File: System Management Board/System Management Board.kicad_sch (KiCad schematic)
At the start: 138 parts, among them IC1 SI2318CDS-T1-GE3, IC2 SI2318CDS-T1-GE3, IC3 SI2318CDS-T1-GE3, IC4 SI2318CDS-T1-GE3, IC5 SI2318CDS-T1-GE3, IC6 SI2318CDS-T1-GE3, J1 Conn_01x04_Male, J10 Conn_01x02_Male, J11 Conn_02x20_Odd_Even, J12 Conn_02x05_Top_Bottom, J13 Conn_01x04_Female, J2 Conn_01x04_Male, J3 Conn_01x02_Male, J4 PJ-063BH, J5 Conn_01x02_Male, J6 Conn_02x06_Counter_Clockwise, J7 Conn_02x20_Odd_Even, J8 Conn_01x02_Male, J9 Conn_01x02_Male, K1 J115F11CH5VDCS61.5U, K2 J114FL1CS165VDC.41, K3 J114FL1CS165VDC.41, SW1 SW_Push, SW2 SW_Push, U1 SC0915, U4 R1560J501B-T1-YE, U5 74HC4051, U6 MCP9700T-ETT, U7 MCP9700T-ETT

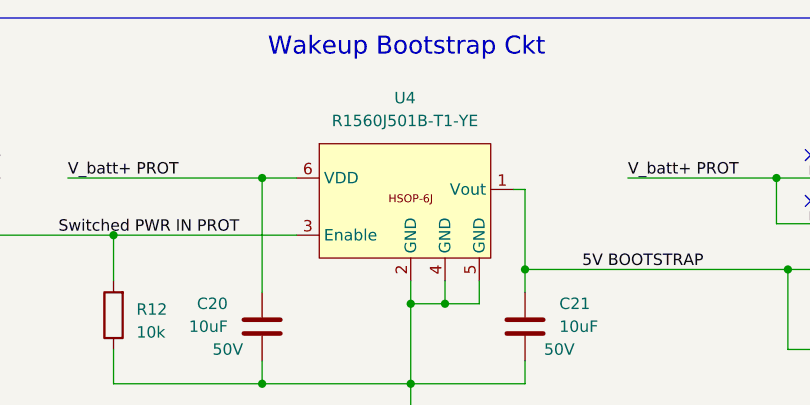
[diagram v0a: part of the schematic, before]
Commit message: minor changes naming or routing
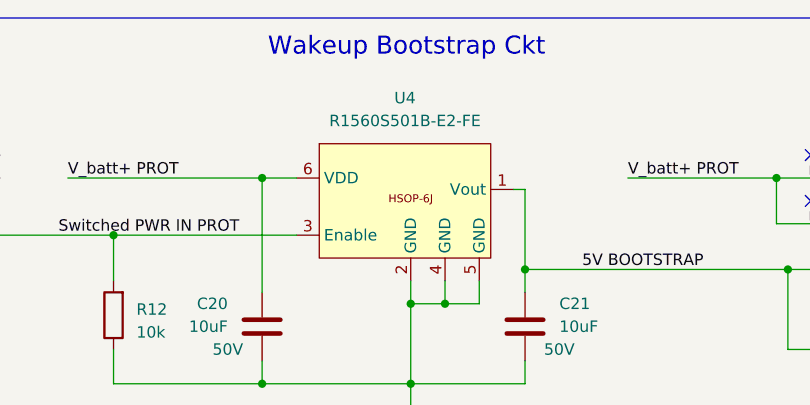
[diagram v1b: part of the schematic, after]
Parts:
- U4: value R1560J501B-T1-YE -> R1560S501B-E2-FE
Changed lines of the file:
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@@
 			)
 		)
-		(property "Value" "R1560J501B-T1-YE"
+		(property "Value" "R1560S501B-E2-FE"
 			(at 164.465 26.67 0)
 			(effects

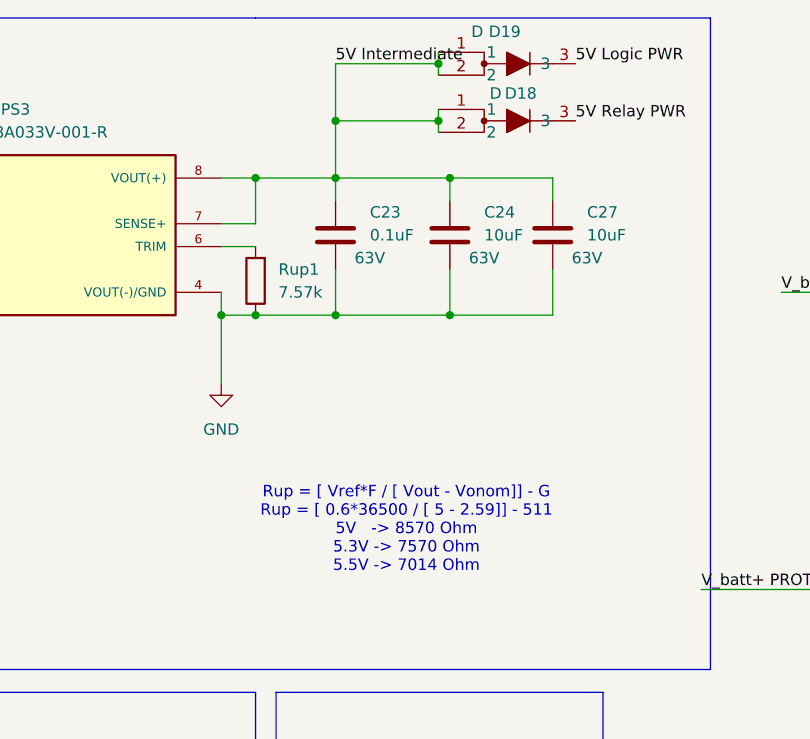
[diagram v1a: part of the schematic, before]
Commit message: ready for review from superiors. 3D models made more complete
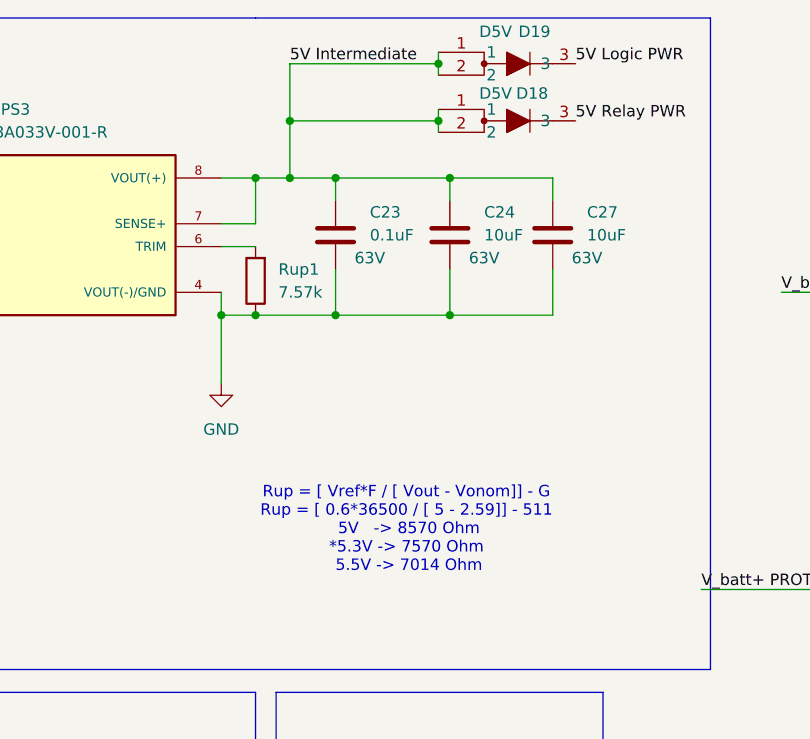
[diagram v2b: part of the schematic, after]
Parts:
- D18, D19: value D -> D5V
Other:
- note added: "Rup = [ Vref*F / [ Vout - Vonom]] - G Rup = [ 0.6*36500 / [ 5 - 2.59]] - 511 5V -> 8570 Ohm *5.3V -> 7570 Ohm 5.5V -> 7014 Ohm"
- note removed: "Rup = [ Vref*F / [ Vout - Vonom]] - G Rup = [ 0.6*36500 / [ 5 - 2.59]] - 511 5V -> 8570 Ohm 5.3V -> 7570 Ohm 5.5V -> 7014 Ohm"
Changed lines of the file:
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@@
 	)
 	(junction
+		(at 306.07 26.67)
+		(diameter 0)
+		(color 0 0 0 0)
+	)
+	(junction
 		(at 519.43 266.7)
 		(diameter 0)
@@
 	)
 	(junction
-		(at 311.15 26.67)
-		(diameter 0)
-		(color 0 0 0 0)
-	)
-	(junction
 		(at 425.45 171.45)
 		(diameter 0)
@@
 	)
 	(junction
+		(at 306.07 33.02)
+		(diameter 0)
+		(color 0 0 0 0)
+	)
+	(junction
 		(at 227.33 33.02)
 		(diameter 0)
@@
 	(wire
 		(pts
+			(xy 306.07 26.67) (xy 322.58 26.67)
+		)
+		(stroke
+			(width 0)
+			(type default)
+		)
+	)
+	(wire
+		(pts
 			(xy 60.96 359.41) (xy 67.31 359.41)
 		)
@@
 		)
 	)
+	(wire
+		(pts
+			(xy 306.07 33.02) (xy 311.15 33.02)
+		)
+		(stroke
+			(width 0)
+			(type default)
+		)
+	)
 	(polyline
 		(pts
@@
 	(wire
 		(pts
-			(xy 311.15 20.32) (xy 311.15 26.67)
+			(xy 306.07 20.32) (xy 306.07 26.67)
 		)
 		(stroke
@@
 	(wire
 		(pts
-			(xy 302.26 33.02) (xy 311.15 33.02)
+			(xy 302.26 33.02) (xy 306.07 33.02)
 		)
 		(stroke
@@
 	(wire
 		(pts
-			(xy 311.15 26.67) (xy 311.15 33.02)
+			(xy 306.07 26.67) (xy 306.07 33.02)
 		)
 		(stroke
@@
 	(wire
 		(pts
-			(xy 322.58 20.32) (xy 311.15 20.32)
+			(xy 322.58 20.32) (xy 306.07 20.32)
 		)
 		(stroke
@@
 	(wire
 		(pts
-			(xy 322.58 26.67) (xy 311.15 26.67)
-		)
-		(stroke
-			(width 0)
-			(type default)
-		)
-	)
-	(wire
-		(pts
 			(xy 105.41 186.69) (xy 105.41 173.99)
 		)
@@
 		)
 	)
-	(text "Rup = [ Vref*F / [ Vout - Vonom]] - G \nRup = [ 0.6*36500 / [ 5 - 2.59]] - 511\n5V   -> 8570 Ohm\n5.3V -> 7570 Ohm\n5.5V -> 7014 Ohm\n"
+	(text "Rup = [ Vref*F / [ Vout - Vonom]] - G \nRup = [ 0.6*36500 / [ 5 - 2.59]] - 511\n 5V   -> 8570 Ohm\n*5.3V -> 7570 Ohm\n 5.5V -> 7014 Ohm\n"
 		(exclude_from_sim no)
 		(at 319.024 72.136 0)
@@
 	)
 	(label "5V Intermediate"
-		(at 311.15 20.32 0)
+		(at 306.07 20.32 0)
 		(fields_autoplaced yes)
 		(effects
@@
 		(dnp no)
 		(property "Reference" "D19"
-			(at 329.946 16.764 0)
+			(at 333.248 16.764 0)
 			(effects
 				(font
@@
 			)
 		)
-		(property "Value" "D"
-			(at 326.898 16.764 0)
+		(property "Value" "D5V"
+			(at 328.93 16.764 0)
 			(effects
 				(font
@@
 		(dnp no)
 		(property "Reference" "D18"
-			(at 331.724 23.622 0)
+			(at 332.994 23.622 0)
 			(effects
 				(font
@@
 			)
 		)
-		(property "Value" "D"
+		(property "Value" "D5V"
 			(at 328.93 23.622 0)
 			(effects

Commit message: Pushing most recent, no significant changes
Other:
- note added: "Rup = [ Vref*F / [ Vout - Vonom]] - G Rup = [ 0.6*36500 / [ 5 - 2.59]] - 511 5V -> 8570 Ohm *5.3V -> 7570 Ohm 5.5V -> 7014 Ohm We selected a 7500 Ohm resistor to order"
- note removed: "Rup = [ Vref*F / [ Vout - Vonom]] - G Rup = [ 0.6*36500 / [ 5 - 2.59]] - 511 5V -> 8570 Ohm *5.3V -> 7570 Ohm 5.5V -> 7014 Ohm"
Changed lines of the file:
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@@
 		)
 	)
-	(text "Rup = [ Vref*F / [ Vout - Vonom]] - G \nRup = [ 0.6*36500 / [ 5 - 2.59]] - 511\n 5V   -> 8570 Ohm\n*5.3V -> 7570 Ohm\n 5.5V -> 7014 Ohm\n"
+	(text "Rup = [ Vref*F / [ Vout - Vonom]] - G \nRup = [ 0.6*36500 / [ 5 - 2.59]] - 511\n 5V   -> 8570 Ohm\n*5.3V -> 7570 Ohm \n 5.5V -> 7014 Ohm \nWe selected a 7500 Ohm resistor to order\n\n"
 		(exclude_from_sim no)
 		(at 319.024 72.136 0)

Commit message: testing points added
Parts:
- added TP2: KeySwitch IN, TestPoint:TestPoint_THTPad_D2.0mm_Drill1.0mm, symbol Connector:TestPoint
- added TP3, TP4, TP5, TP6: TestPoint, TestPoint:TestPoint_THTPad_D2.0mm_Drill1.0mm, symbol Connector:TestPoint
- R21, R25, R27, R29: value 100k -> 220k
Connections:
- net 15v PWR: now also TP5.1
- net 48V PWR: now also TP6.1
- net 5V BOOTSTRAP: now also TP3.1
- net 5V Intermediate: now also TP4.1
- net KeySwitch IN: now also TP2.1

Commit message: pushing all test pt mods
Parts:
- renumbered TP2 to TP1, TP3 to TP2, TP4 to TP3, TP5 to TP4, TP6 to TP5
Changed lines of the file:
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@@
 		(dnp no)
 		(fields_autoplaced yes)
-		(property "Reference" "TP5"
+		(property "Reference" "TP4"
 			(at 563.88 262.1279 0)
 			(effects
@@
 			(project "System Management Board"
 				(path "/49025907-9104-48d6-bcc4-645bc95bc4a8"
-					(reference "TP5")
+					(reference "TP4")
 					(unit 1)
 				)
@@
 		(dnp no)
 		(fields_autoplaced yes)
-		(property "Reference" "TP4"
+		(property "Reference" "TP3"
 			(at 302.768 21.59 90)
 			(effects
@@
 			(project "System Management Board"
 				(path "/49025907-9104-48d6-bcc4-645bc95bc4a8"
-					(reference "TP4")
+					(reference "TP3")
 					(unit 1)
 				)
@@
 		(dnp no)
 		(fields_autoplaced yes)
-		(property "Reference" "TP6"
+		(property "Reference" "TP5"
 			(at 563.88 319.2779 0)
 			(effects
@@
 			(project "System Management Board"
 				(path "/49025907-9104-48d6-bcc4-645bc95bc4a8"
-					(reference "TP6")
+					(reference "TP5")
 					(unit 1)
 				)
@@
 		(dnp no)
 		(fields_autoplaced yes)
-		(property "Reference" "TP3"
+		(property "Reference" "TP2"
 			(at 209.55 38.6079 0)
 			(effects
@@
 			(project "System Management Board"
 				(path "/49025907-9104-48d6-bcc4-645bc95bc4a8"
-					(reference "TP3")
+					(reference "TP2")
 					(unit 1)
 				)
@@
 		(dnp no)
 		(fields_autoplaced yes)
-		(property "Reference" "TP2"
+		(property "Reference" "TP1"
 			(at 66.04 24.6379 0)
 			(effects
@@
 			(project "System Management Board"
 				(path "/49025907-9104-48d6-bcc4-645bc95bc4a8"
-					(reference "TP2")
+					(reference "TP1")
 					(unit 1)
 				)

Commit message: significant amount of testing points added
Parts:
- added TP10, TP11, TP12, TP13, TP14, TP6, TP7, TP8, TP9: TestPoint, TestPoint:TestPoint_Pad_D1.0mm, symbol Connector:TestPoint
- C20, C21: Voltage 50V -> 63V
- TP1, TP2, TP3, TP4, TP5: footprint TestPoint:TestPoint_THTPad_D2.0mm_Drill1.0mm -> TestPoint:TestPoint_Pad_D1.0mm
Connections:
- net Aux_ADC_IN: now also TP7.1
- net COMP_Vout MES_ADC: now also TP8.1
- net KeySW_Vin MES_ADC: now also TP6.1
- net Light_A_Vout MES_ADC: now also TP10.1
- net Light_B_Vout MES_ADC: now also TP12.1
- net PICO 3V3: now also TP14.1
- net POE_SW_Vout MES_ADC: now also TP13.1
- net TEMP_SENSE_1: now also TP9.1
- net TEMP_SENSE_2: now also TP11.1
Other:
- note added: "Testing Points"
- moved on the sheet: F4, F5, F8, F9, R13, R14, R15, R16, R17, R18, R19, R20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

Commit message: removed J5, moved J9 for clearance, removed global flags
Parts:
- removed J5: Conn_01x02_Male, SMB:1843606, symbol Connector:Conn_01x02_Male
